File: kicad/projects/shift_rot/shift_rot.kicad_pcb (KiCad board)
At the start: 2 copper layers, 203.2 x 97.8 mm, 47 parts, among them J4 Conn_01x03_Pin, J5 Conn_01x16_Socket, J6 Conn_01x02_Socket, J7 Control_signal_backplane, J8 Bus_connection, J9 Aux_connection, U10 74HC08, U11 74HC574, U12 74HC574, U13 74HC138, U14 74HC157, U16 74HC245, U17 74HC245, U18 74HC02, U19 74HC00, U20 74HC377, U21 74HC377, U3 74HC245, U4 74HC245, U5 74HC245, U6 74HC245, U7 74HC245, U8 74HC245, U9 74HC157

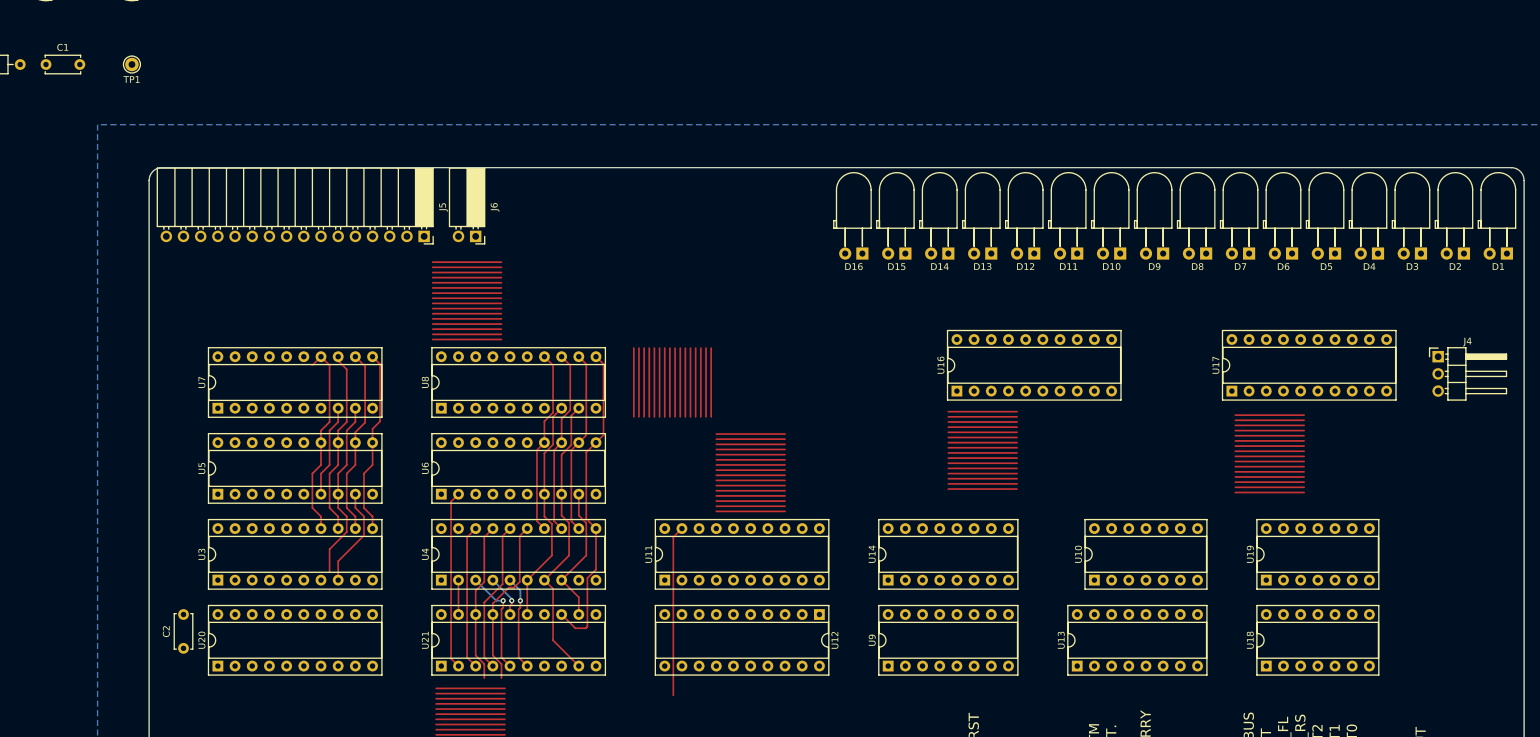
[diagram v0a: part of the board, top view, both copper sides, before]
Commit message: Schematic mostly done for shift rot.
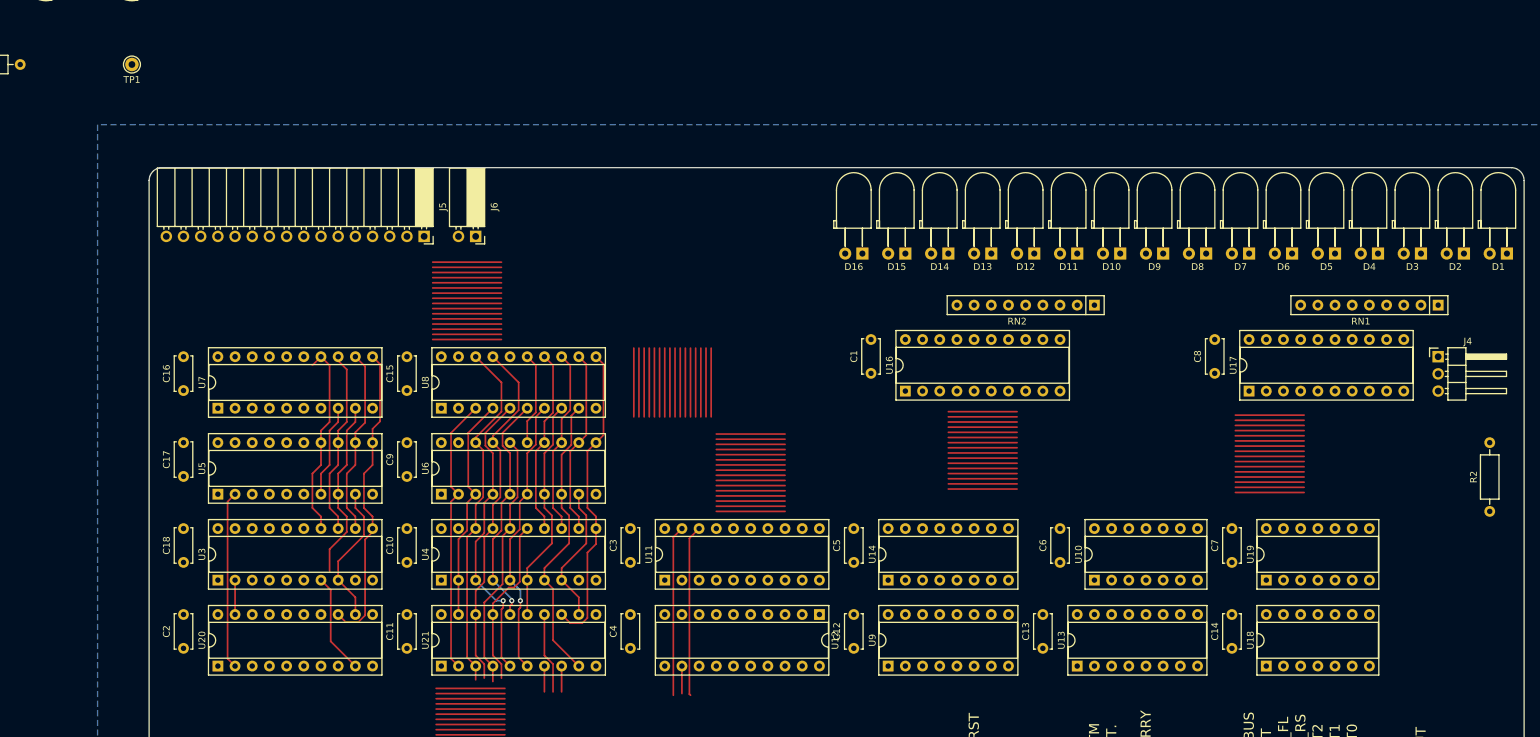
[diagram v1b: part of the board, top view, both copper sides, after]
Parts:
- added C10: C, Capacitor_THT:C_Disc_D5.0mm_W2.5mm_P5.00mm, F.Cu at (88.9, 109.1)
- added C11: C, Capacitor_THT:C_Disc_D5.0mm_W2.5mm_P5.00mm, F.Cu at (88.9, 121.8)
- added C12: C, Capacitor_THT:C_Disc_D5.0mm_W2.5mm_P5.00mm, F.Cu at (154.9, 121.8)
- added C13: C, Capacitor_THT:C_Disc_D5.0mm_W2.5mm_P5.00mm, F.Cu at (182.9, 121.8)
- added C14: C, Capacitor_THT:C_Disc_D5.0mm_W2.5mm_P5.00mm, F.Cu at (210.8, 121.8)
- added C15: C, Capacitor_THT:C_Disc_D5.0mm_W2.5mm_P5.00mm, F.Cu at (88.9, 83.7)
- added C16: C, Capacitor_THT:C_Disc_D5.0mm_W2.5mm_P5.00mm, F.Cu at (55.9, 83.7)
- added C17: C, Capacitor_THT:C_Disc_D5.0mm_W2.5mm_P5.00mm, F.Cu at (55.9, 96.4)
- added C18: C, Capacitor_THT:C_Disc_D5.0mm_W2.5mm_P5.00mm, F.Cu at (55.9, 109.1)
- added C3: C, Capacitor_THT:C_Disc_D5.0mm_W2.5mm_P5.00mm, F.Cu at (121.9, 109.1)
- added C4: C, Capacitor_THT:C_Disc_D5.0mm_W2.5mm_P5.00mm, F.Cu at (121.9, 121.8)
- added C5: C, Capacitor_THT:C_Disc_D5.0mm_W2.5mm_P5.00mm, F.Cu at (154.9, 109.1)
- added C6: C, Capacitor_THT:C_Disc_D5.0mm_W2.5mm_P5.00mm, F.Cu at (185.4, 109.1)
- added C7: C, Capacitor_THT:C_Disc_D5.0mm_W2.5mm_P5.00mm, F.Cu at (210.8, 109.1)
- added C8: C, Capacitor_THT:C_Disc_D5.0mm_W2.5mm_P5.00mm, F.Cu at (208.3, 81.2)
- added C9: C, Capacitor_THT:C_Disc_D5.0mm_W2.5mm_P5.00mm, F.Cu at (88.9, 96.4)
- added R2: 10K, Resistor_THT:R_Axial_DIN0207_L6.3mm_D2.5mm_P10.16mm_Horizontal, F.Cu at (248.9, 101.6)
- added RN1: R_Network08_US, Resistor_THT:R_Array_SIP9, F.Cu at (241.3, 71.1)
- added RN2: R_Network08_US, Resistor_THT:R_Array_SIP9, F.Cu at (190.5, 71.1)
- moved C1 130.2 mm to (157.5, 81.2), turned to 90 degrees
- moved U16 7.62 mm to (162.6, 83.8)
- moved U17 2.54 mm to (213.4, 83.8)
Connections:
- net Net-(U11-Cp) renamed /SAFE_POPPED_CLK
- D1 pad 1: unconnected-(D1-K-Pad1) -> Net-(D1-K)
- D1 pad 2: unconnected-(D1-A-Pad2) -> Net-(D1-A)
- D10 pad 1: unconnected-(D10-K-Pad1) -> Net-(D10-K)
- D10 pad 2: unconnected-(D10-A-Pad2) -> Net-(D10-A)
- D11 pad 1: unconnected-(D11-K-Pad1) -> Net-(D11-K)
- D11 pad 2: unconnected-(D11-A-Pad2) -> Net-(D11-A)
- D12 pad 1: unconnected-(D12-K-Pad1) -> Net-(D12-K)
- D12 pad 2: unconnected-(D12-A-Pad2) -> Net-(D12-A)
- D13 pad 1: unconnected-(D13-K-Pad1) -> Net-(D13-K)
- D13 pad 2: unconnected-(D13-A-Pad2) -> Net-(D13-A)
- D14 pad 1: unconnected-(D14-K-Pad1) -> Net-(D14-K)
- D14 pad 2: unconnected-(D14-A-Pad2) -> Net-(D14-A)
- D15 pad 1: unconnected-(D15-K-Pad1) -> Net-(D15-K)
- D15 pad 2: unconnected-(D15-A-Pad2) -> Net-(D15-A)
- D16 pad 1: unconnected-(D16-K-Pad1) -> Net-(D16-K)
- D16 pad 2: unconnected-(D16-A-Pad2) -> Net-(D16-A)
- D2 pad 1: unconnected-(D2-K-Pad1) -> Net-(D2-K)
- D2 pad 2: unconnected-(D2-A-Pad2) -> Net-(D2-A)
- D3 pad 1: unconnected-(D3-K-Pad1) -> Net-(D3-K)
- D3 pad 2: unconnected-(D3-A-Pad2) -> Net-(D3-A)
- D4 pad 1: unconnected-(D4-K-Pad1) -> Net-(D4-K)
- D4 pad 2: unconnected-(D4-A-Pad2) -> Net-(D4-A)
- D5 pad 1: unconnected-(D5-K-Pad1) -> Net-(D5-K)
- D5 pad 2: unconnected-(D5-A-Pad2) -> Net-(D5-A)
- D6 pad 1: unconnected-(D6-K-Pad1) -> Net-(D6-K)
- D6 pad 2: unconnected-(D6-A-Pad2) -> Net-(D6-A)
- D7 pad 1: unconnected-(D7-K-Pad1) -> Net-(D7-K)
- D7 pad 2: unconnected-(D7-A-Pad2) -> Net-(D7-A)
- D8 pad 1: unconnected-(D8-K-Pad1) -> Net-(D8-K)
- D8 pad 2: unconnected-(D8-A-Pad2) -> Net-(D8-A)
- D9 pad 1: unconnected-(D9-K-Pad1) -> Net-(D9-K)
- D9 pad 2: unconnected-(D9-A-Pad2) -> Net-(D9-A)
- J4 pad 1: unconnected-(J4-Pin_1-Pad1) -> VCC
- J4 pad 2: unconnected-(J4-Pin_2-Pad2) -> Net-(J4-Pin_2)
- J4 pad 3: unconnected-(J4-Pin_3-Pad3) -> GND
- J5 pad 1: unconnected-(J5-Pin_1-Pad1) -> /CNTNT_0
- J5 pad 10: unconnected-(J5-Pin_10-Pad10) -> /CNTNT_9
- J5 pad 11: unconnected-(J5-Pin_11-Pad11) -> /CNTNT_10
- J5 pad 12: unconnected-(J5-Pin_12-Pad12) -> /CNTNT_11
- J5 pad 13: unconnected-(J5-Pin_13-Pad13) -> /CNTNT_12
- J5 pad 14: unconnected-(J5-Pin_14-Pad14) -> /CNTNT_13
- J5 pad 15: unconnected-(J5-Pin_15-Pad15) -> /CNTNT_14
- J5 pad 16: unconnected-(J5-Pin_16-Pad16) -> /CNTNT_15
- J5 pad 2: unconnected-(J5-Pin_2-Pad2) -> /CNTNT_1
- J5 pad 3: unconnected-(J5-Pin_3-Pad3) -> /CNTNT_2
- J5 pad 4: unconnected-(J5-Pin_4-Pad4) -> /CNTNT_3
- J5 pad 5: unconnected-(J5-Pin_5-Pad5) -> /CNTNT_4
- J5 pad 6: unconnected-(J5-Pin_6-Pad6) -> /CNTNT_5
- J5 pad 7: unconnected-(J5-Pin_7-Pad7) -> /CNTNT_6
- J5 pad 8: unconnected-(J5-Pin_8-Pad8) -> /CNTNT_7
- J5 pad 9: unconnected-(J5-Pin_9-Pad9) -> /CNTNT_8
- J7 pad 30: unconnected-(J7-SFT0-Pad30) -> /SFT_0
- J7 pad 31: unconnected-(J7-SFT1-Pad31) -> /SFT_1
- J7 pad 32: unconnected-(J7-SFT2-Pad32) -> /SFT_2
- U10 pad 14: unconnected-(U10E-VCC-Pad14) -> VCC
- U10 pad 7: unconnected-(U10E-GND-Pad7) -> GND
- U11 pad 10: unconnected-(U11-GND-Pad10) -> GND
- U11 pad 20: unconnected-(U11-VCC-Pad20) -> VCC
- U12 pad 10: unconnected-(U12-GND-Pad10) -> GND
- U12 pad 20: unconnected-(U12-VCC-Pad20) -> VCC
- U13 pad 1: unconnected-(U13-A-Pad1) -> /SFT_0
- U13 pad 16: unconnected-(U13-VCC-Pad16) -> VCC
- U13 pad 2: unconnected-(U13-B-Pad2) -> /SFT_1
- U13 pad 3: unconnected-(U13-C-Pad3) -> /SFT_2
- U13 pad 4: unconnected-(U13-~{G2A}-Pad4) -> GND
- U13 pad 5: unconnected-(U13-~{G2B}-Pad5) -> GND
- U13 pad 6: unconnected-(U13-G1-Pad6) -> VCC
- U13 pad 8: unconnected-(U13-GND-Pad8) -> GND
- U14 pad 16: unconnected-(U14-VCC-Pad16) -> VCC
- U14 pad 8: unconnected-(U14-GND-Pad8) -> GND
- U16 pad 1: unconnected-(U16-DIR-Pad1) -> VCC
- U16 pad 10: unconnected-(U16-GND-Pad10) -> GND
- U16 pad 11: unconnected-(U16-B8-Pad11) -> Net-(D9-A)
- U16 pad 12: unconnected-(U16-B7-Pad12) -> Net-(D10-A)
- U16 pad 13: unconnected-(U16-B6-Pad13) -> Net-(D11-A)
- U16 pad 14: unconnected-(U16-B5-Pad14) -> Net-(D12-A)
- U16 pad 15: unconnected-(U16-B4-Pad15) -> Net-(D13-A)
- U16 pad 16: unconnected-(U16-B3-Pad16) -> Net-(D14-A)
- U16 pad 17: unconnected-(U16-B2-Pad17) -> Net-(D15-A)
- U16 pad 18: unconnected-(U16-B1-Pad18) -> Net-(D16-A)
- U16 pad 19: unconnected-(U16-~{OE}-Pad19) -> Net-(J4-Pin_2)
- U16 pad 2: unconnected-(U16-A1-Pad2) -> /CNTNT_15
- U16 pad 20: unconnected-(U16-VCC-Pad20) -> VCC
- U16 pad 3: unconnected-(U16-A2-Pad3) -> /CNTNT_14
- U16 pad 4: unconnected-(U16-A3-Pad4) -> /CNTNT_13
- U16 pad 5: unconnected-(U16-A4-Pad5) -> /CNTNT_12
- U16 pad 6: unconnected-(U16-A5-Pad6) -> /CNTNT_11
- U16 pad 7: unconnected-(U16-A6-Pad7) -> /CNTNT_10
- U16 pad 8: unconnected-(U16-A7-Pad8) -> /CNTNT_9
- U16 pad 9: unconnected-(U16-A8-Pad9) -> /CNTNT_8
- U17 pad 1: unconnected-(U17-DIR-Pad1) -> VCC
- U17 pad 10: unconnected-(U17-GND-Pad10) -> GND
- U17 pad 11: unconnected-(U17-B8-Pad11) -> Net-(D1-A)
- U17 pad 12: unconnected-(U17-B7-Pad12) -> Net-(D2-A)
- U17 pad 13: unconnected-(U17-B6-Pad13) -> Net-(D3-A)
- U17 pad 14: unconnected-(U17-B5-Pad14) -> Net-(D4-A)
- U17 pad 15: unconnected-(U17-B4-Pad15) -> Net-(D5-A)
- U17 pad 16: unconnected-(U17-B3-Pad16) -> Net-(D6-A)
- U17 pad 17: unconnected-(U17-B2-Pad17) -> Net-(D7-A)
- U17 pad 18: unconnected-(U17-B1-Pad18) -> Net-(D8-A)
- U17 pad 19: unconnected-(U17-~{OE}-Pad19) -> Net-(J4-Pin_2)
- U17 pad 2: unconnected-(U17-A1-Pad2) -> /CNTNT_7
- U17 pad 20: unconnected-(U17-VCC-Pad20) -> VCC
- U17 pad 3: unconnected-(U17-A2-Pad3) -> /CNTNT_6
- U17 pad 4: unconnected-(U17-A3-Pad4) -> /CNTNT_5
- U17 pad 5: unconnected-(U17-A4-Pad5) -> /CNTNT_4
- U17 pad 6: unconnected-(U17-A5-Pad6) -> /CNTNT_3
- U17 pad 7: unconnected-(U17-A6-Pad7) -> /CNTNT_2
- U17 pad 8: unconnected-(U17-A7-Pad8) -> /CNTNT_1
- U17 pad 9: unconnected-(U17-A8-Pad9) -> /CNTNT_0
- U18 pad 14: unconnected-(U18E-VCC-Pad14) -> VCC
- U18 pad 7: unconnected-(U18E-GND-Pad7) -> GND
- U19 pad 10: unconnected-(U19-Pad10) -> VCC
- U19 pad 12: unconnected-(U19-Pad12) -> VCC
- U19 pad 13: unconnected-(U19-Pad13) -> VCC
- U19 pad 14: unconnected-(U19E-VCC-Pad14) -> VCC
- U19 pad 4: unconnected-(U19-Pad4) -> VCC
- U19 pad 5: unconnected-(U19-Pad5) -> VCC
- U19 pad 7: unconnected-(U19E-GND-Pad7) -> GND
- U19 pad 9: unconnected-(U19-Pad9) -> VCC
- U20 pad 11: Net-(U20-CP) -> /DATA_CLK
- U20 pad 12: /CNTNT_11 -> /CNTNT_8
- U20 pad 13: /BUS_11 -> /BUS_8
- U20 pad 16: /CNTNT_9 -> /CNTNT_12
- U20 pad 17: /BUS_9 -> /BUS_12
- U20 pad 18: /BUS_8 -> /BUS_14
- U20 pad 19: /CNTNT_8 -> /CNTNT_14
- U20 pad 4: /BUS_14 -> /BUS_13
- U20 pad 5: /CNTNT_14 -> /CNTNT_13
- U20 pad 6: /CNTNT_13 -> /CNTNT_11
- U20 pad 7: /BUS_13 -> /BUS_11
- U20 pad 8: /BUS_12 -> /BUS_9
- U20 pad 9: /CNTNT_12 -> /CNTNT_9
- U21 pad 11: Net-(U20-CP) -> /DATA_CLK
- U3 pad 10: unconnected-(U3-GND-Pad10) -> GND
- U3 pad 20: unconnected-(U3-VCC-Pad20) -> VCC
- U4 pad 10: unconnected-(U4-GND-Pad10) -> GND
- U4 pad 20: unconnected-(U4-VCC-Pad20) -> VCC
- U5 pad 10: unconnected-(U5-GND-Pad10) -> GND
- U5 pad 20: unconnected-(U5-VCC-Pad20) -> VCC
- U6 pad 10: unconnected-(U6-GND-Pad10) -> GND
- U6 pad 20: unconnected-(U6-VCC-Pad20) -> VCC
- U7 pad 10: unconnected-(U7-GND-Pad10) -> GND
- U7 pad 20: unconnected-(U7-VCC-Pad20) -> VCC
- U8 pad 10: unconnected-(U8-GND-Pad10) -> GND
- U8 pad 20: unconnected-(U8-VCC-Pad20) -> VCC
- U9 pad 16: unconnected-(U9-VCC-Pad16) -> VCC
- U9 pad 8: unconnected-(U9-GND-Pad8) -> GND
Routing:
- net /BUS_7: track 21.4 -> 52.9 mm
- net /BUS_6: track 23.7 -> 53.1 mm
- net /CNTNT_4: track 6.34 -> 34.8 mm
- net /CNTNT_6: track 5.08 -> 33.5 mm
- net /CNTNT_5: track 15.6 -> 44.0 mm
- net /CNTNT_3: track 14.0 -> 41.5 mm
- net /CNTNT_15: track 0.00 -> 26.3 mm
- net /BUS_14: track 0.00 -> 25.3 mm
- net /SAFE_POPPED_CLK: track 20.3 -> 0.00 mm
- net (no net): track 955.0 -> 975.4 mm
- net /BUS_8: track 27.4 -> 45.5 mm
- net /BUS_5: track 22.4 -> 38.3 mm
- net /CNTNT_9: track 26.8 -> 41.6 mm
- net /CNTNT_7: track 26.3 -> 41.0 mm
- net /BUS_4: track 25.2 -> 38.9 mm
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
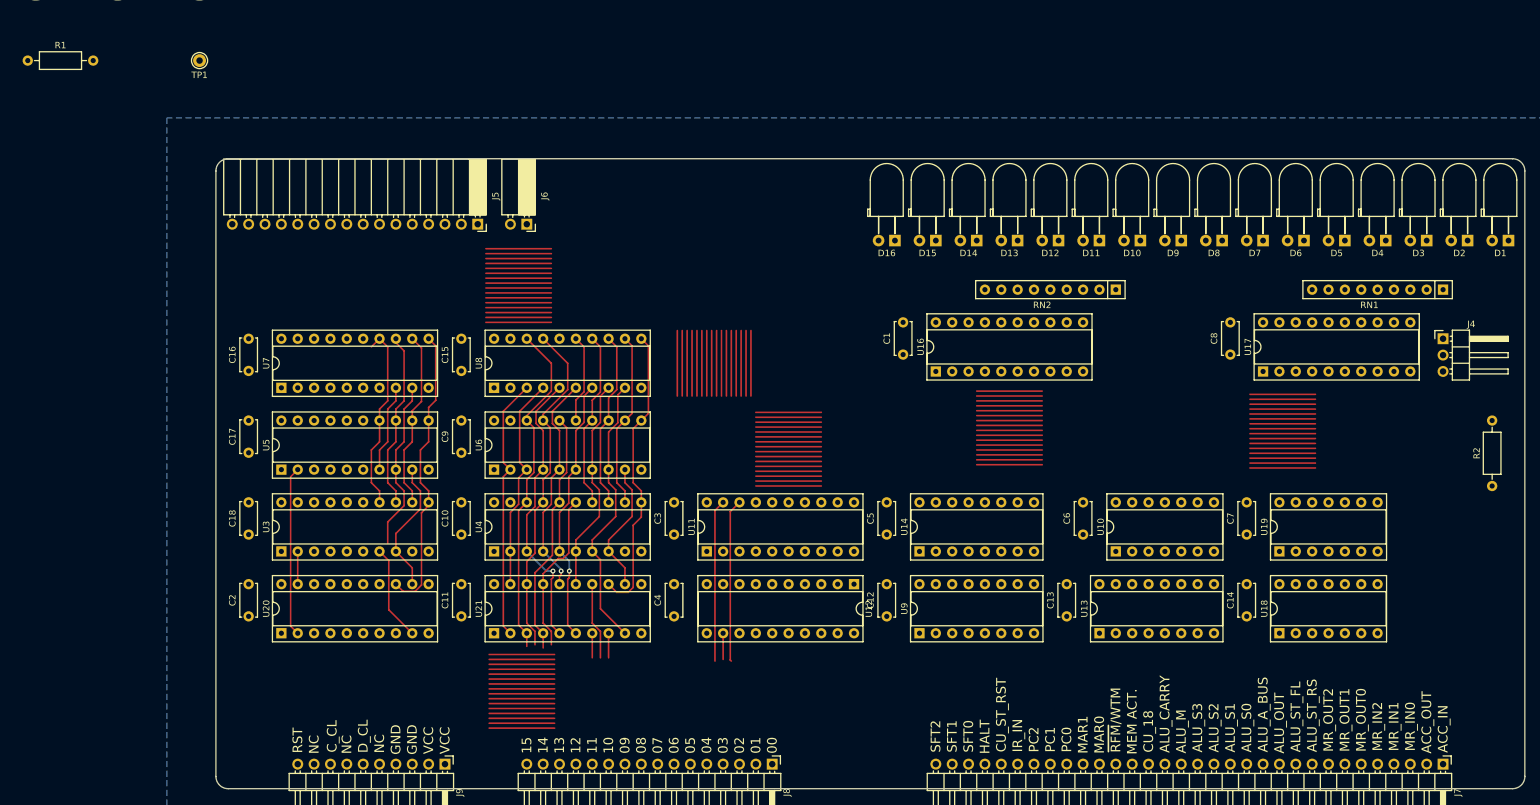
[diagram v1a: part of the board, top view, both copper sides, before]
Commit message: More PCB work on shift rot
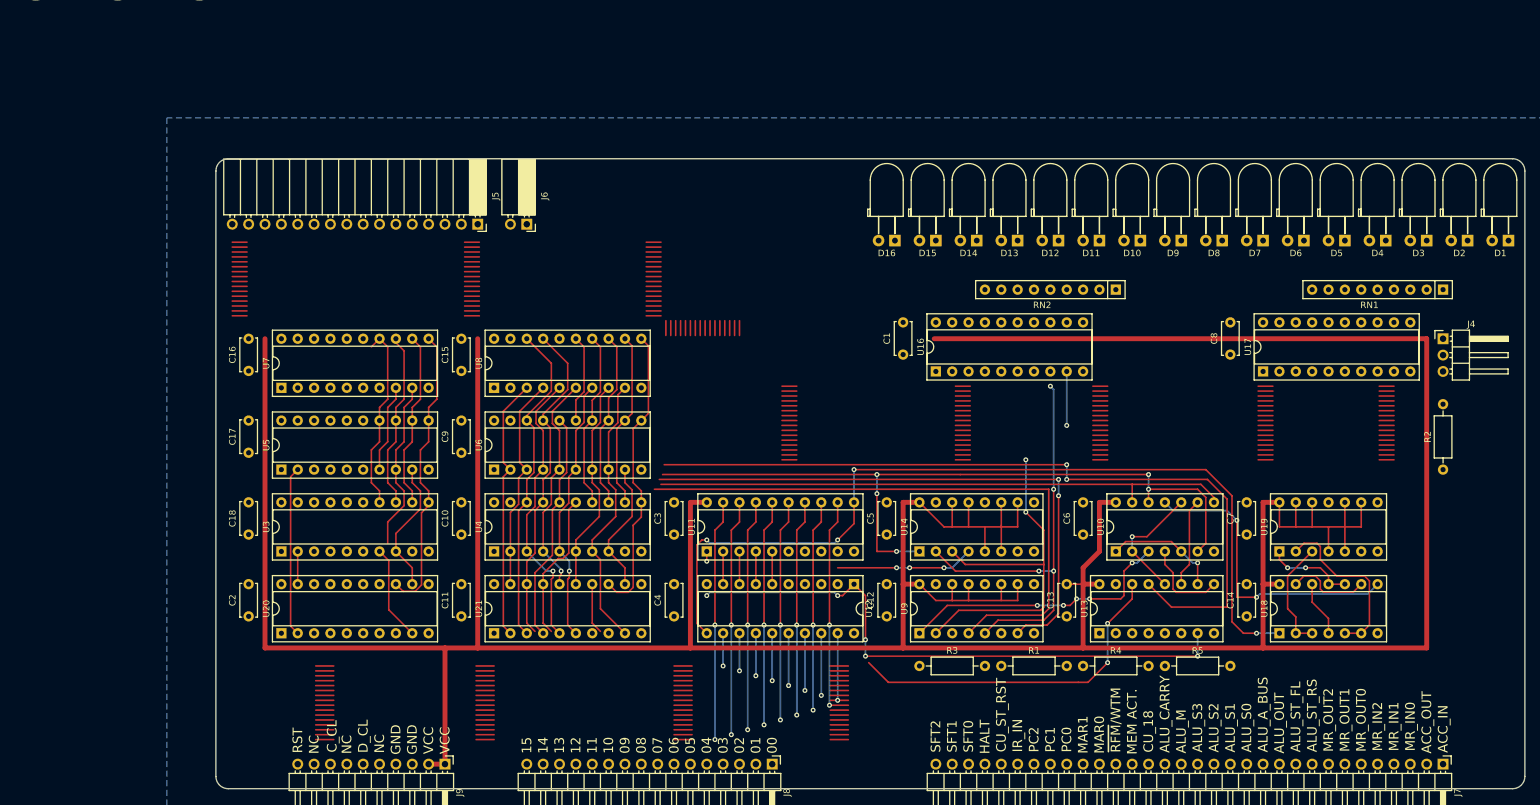
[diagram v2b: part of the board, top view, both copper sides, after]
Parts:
- removed TP1: TestPoint, Connector_Pin:Pin_D1.0mm_L10.0mm
- added R3: 10K, Resistor_THT:R_Axial_DIN0207_L6.3mm_D2.5mm_P10.16mm_Horizontal, F.Cu at (160.0, 129.5)
- added R4: 10K, Resistor_THT:R_Axial_DIN0207_L6.3mm_D2.5mm_P10.16mm_Horizontal, F.Cu at (185.4, 129.5)
- added R5: 10K, Resistor_THT:R_Axial_DIN0207_L6.3mm_D2.5mm_P10.16mm_Horizontal, F.Cu at (198.1, 129.5)
- R1: value R_US -> 10K
- moved R1 178.0 mm to (172.7, 129.5)
- moved R2 8.03 mm to (241.3, 99.1)
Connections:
- net /~{EITHER_LEFT_OR_EITHER_RIGHT} renamed /~{EITHER_LEFT_OR_RIGHT_OUT}
- net /~{EITHER_ROTATE} renamed /~{EITHER_ROTATE_OUT}
- R1 pad 2: GND -> /~{EITHER_LEFT_OUT}
- U10 pad 12: /~{EITHER_LEFT} -> /~{EITHER_RIGHT_OUT}
- U10 pad 13: /~{EITHER_RIGHT} -> /~{EITHER_LEFT_OUT}
- U10 pad 6: /~{EITHER_LEFT} -> /~{EITHER_RIGHT_OUT}
- U10 pad 8: /~{EITHER_RIGHT} -> /~{EITHER_LEFT_OUT}
- U14 pad 1: /~{EITHER_LEFT} -> /~{EITHER_RIGHT_OUT}
- U14 pad 15: unconnected-(U14-~{G}-Pad15) -> GND
- U14 pad 2: /CNTNT_15 -> /CNTNT_0
- U14 pad 3: /CNTNT_0 -> /CNTNT_15
- U3 pad 1: unconnected-(U3-DIR-Pad1) -> VCC
- U3 pad 19: /~{EITHER_LEFT} -> /~{EITHER_LEFT_OUT}
- U4 pad 1: unconnected-(U4-DIR-Pad1) -> VCC
- U4 pad 19: /~{EITHER_LEFT} -> /~{EITHER_LEFT_OUT}
- U5 pad 1: unconnected-(U5-DIR-Pad1) -> VCC
- U6 pad 1: unconnected-(U6-DIR-Pad1) -> VCC
- U7 pad 1: unconnected-(U7-DIR-Pad1) -> VCC
- U7 pad 19: /~{EITHER_RIGHT} -> /~{EITHER_RIGHT_OUT}
- U8 pad 1: unconnected-(U8-DIR-Pad1) -> VCC
- U8 pad 19: /~{EITHER_RIGHT} -> /~{EITHER_RIGHT_OUT}
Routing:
- net (no net): track 975.4 -> 0.00 mm
- net VCC: track 0.00 -> 638.7 mm
- net /SAFE_POPPED_CLK: track 0.00 -> 136.9 mm, vias 0 -> 4
- net /~{STRAIGHT_OUT}: track 0.00 -> 121.4 mm, vias 0 -> 2
- net /~{EITHER_RIGHT_OUT}: track 0.00 -> 116.6 mm, vias 0 -> 5
- net /LEFT_LSB: track 0.00 -> 93.8 mm
- net /~{POPPED_BIT_OUT}: track 0.00 -> 92.6 mm, vias 0 -> 6
- net /RIGHT_MSB: track 0.00 -> 90.4 mm, vias 0 -> 2
- net /~{EITHER_LEFT_OUT}: track 0.00 -> 90.2 mm
- net /CNTNT_0: track 20.8 -> 108.1 mm, vias 0 -> 4
- net /CNTNT_15: track 26.3 -> 104.4 mm, vias 0 -> 2
- net /~{IN}: track 0.00 -> 53.4 mm, vias 0 -> 2
- net /BUS_13: track 0.00 -> 47.0 mm, vias 0 -> 2
- net /~{EITHER_LEFT_OR_RIGHT_OUT}: track 0.00 -> 47.0 mm, vias 0 -> 2
- net /BUS_12: track 0.00 -> 46.2 mm, vias 0 -> 2
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
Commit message: Work on shift rot PCB
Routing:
- net /CNTNT_13: track 20.6 -> 74.8 mm, vias 0 -> 1
- net /BUS_14: track 47.8 -> 99.5 mm, vias 2 -> 4
- net /CNTNT_11: track 20.6 -> 72.3 mm
- net /BUS_12: track 46.2 -> 97.7 mm
- net /BUS_13: track 47.0 -> 96.9 mm
- net /BUS_15: track 48.5 -> 97.4 mm
- net /CNTNT_12: track 20.6 -> 64.4 mm
- net /CNTNT_14: track 25.7 -> 65.9 mm, vias 0 -> 2
- net /POPPED_BIT: track 41.7 -> 80.1 mm, vias 3 -> 11
- net /CNTNT_15: track 104.4 -> 138.6 mm
- net /CNTNT_10: track 34.3 -> 63.6 mm
- net /BUS_3: track 46.0 -> 70.7 mm, vias 1 -> 3
- net /BUS_1: track 44.4 -> 69.1 mm, vias 1 -> 2
- net /BUS_9: track 71.5 -> 96.0 mm, vias 2 -> 3
- net /BUS_10: track 72.2 -> 96.2 mm
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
